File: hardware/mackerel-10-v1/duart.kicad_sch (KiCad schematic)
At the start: 7 parts, among them J2 Conn_01x06, J3 Conn_01x06, U7 XR68C681, X2 3.6864MHz

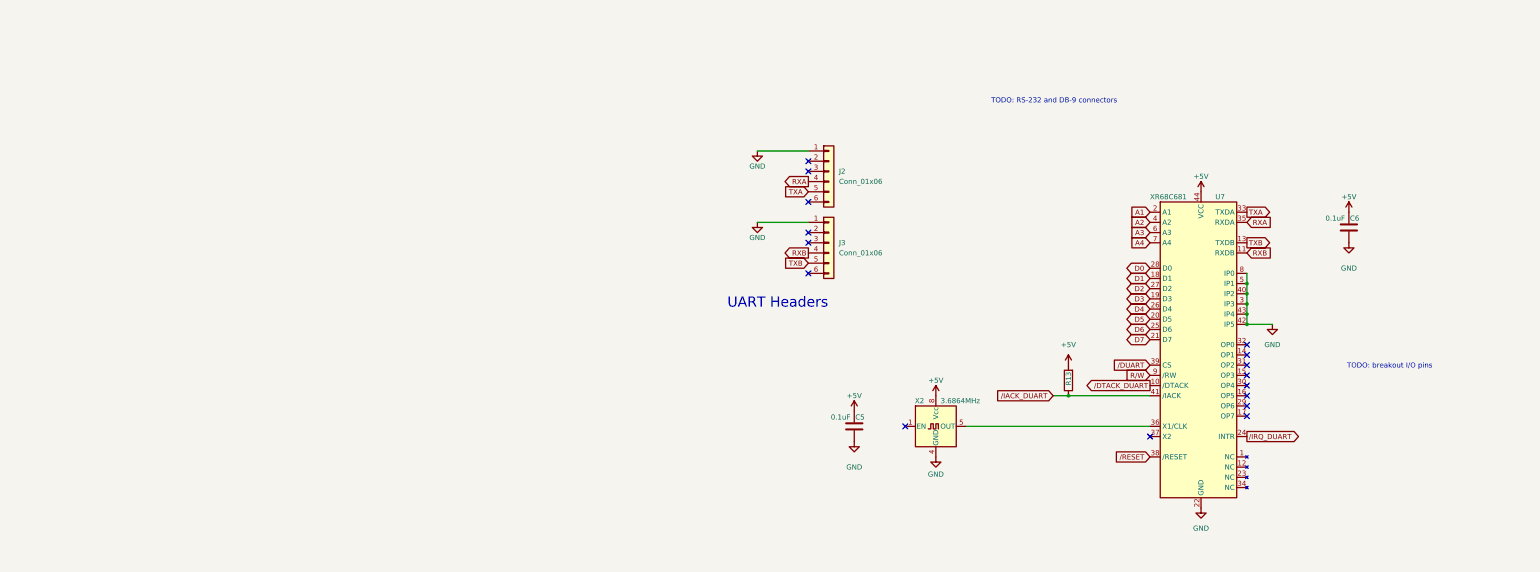
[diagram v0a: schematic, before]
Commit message: Rough layout of components on PCB
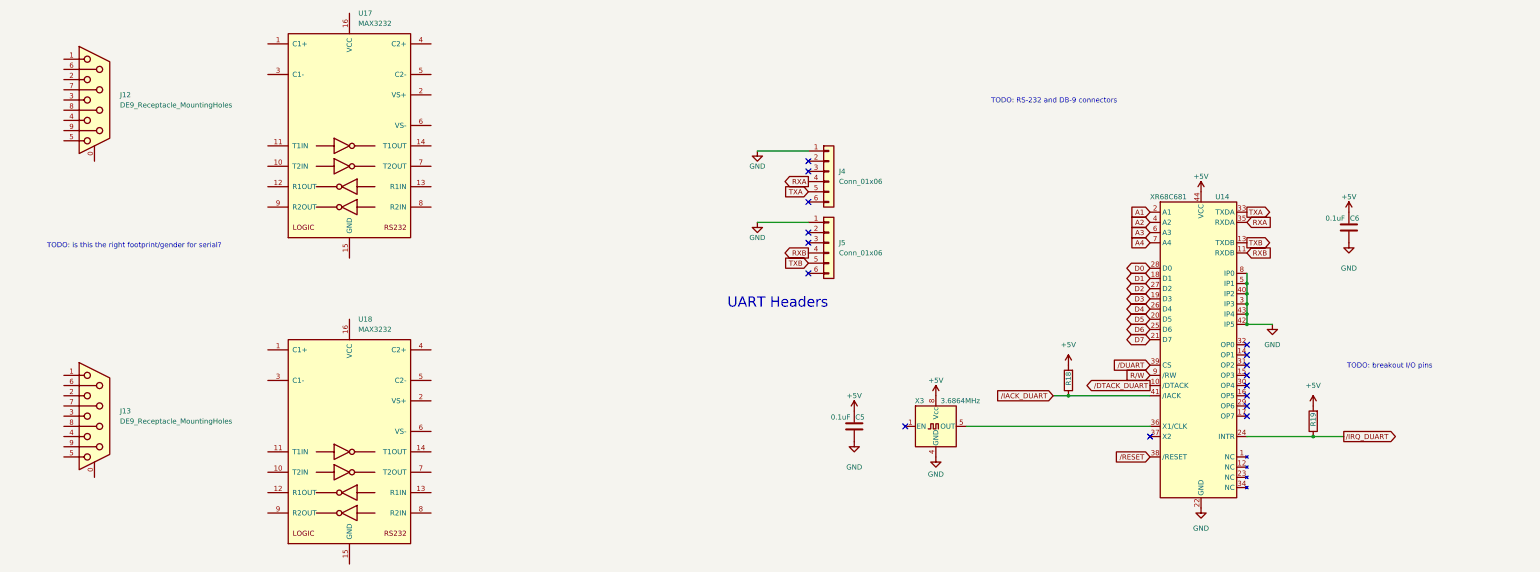
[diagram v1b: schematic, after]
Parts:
- added J12, J13: DE9_Receptacle_MountingHoles, Connector_Dsub:DSUB-9_Female_Horizontal_P2.77x2.84mm_EdgePinOffset7.70mm_Housed_MountingHolesOffset9.12mm, symbol Connector:DE9_Receptacle_MountingHoles
- added R19: R, Resistor_THT:R_Axial_DIN0207_L6.3mm_D2.5mm_P7.62mm_Horizontal, symbol Device:R
- added U17, U18: MAX3232, Package_DIP:DIP-16_W7.62mm_Socket, symbol Interface_UART:MAX3232
- R18: renamed from R13; footprint Resistor_THT:R_Axial_DIN0204_L3.6mm_D1.6mm_P5.08mm_Horizontal -> Resistor_THT:R_Axial_DIN0207_L6.3mm_D2.5mm_P7.62mm_Horizontal
- renumbered J2 to J4, J3 to J5, U7 to U14, X2 to X3
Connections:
- net +5V: now also R19.2
- net /IRQ_DUART: now also R19.1
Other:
- note added: "TODO: is this the right footprint/gender for serial?"

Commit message: Settled on mini ITX form factor
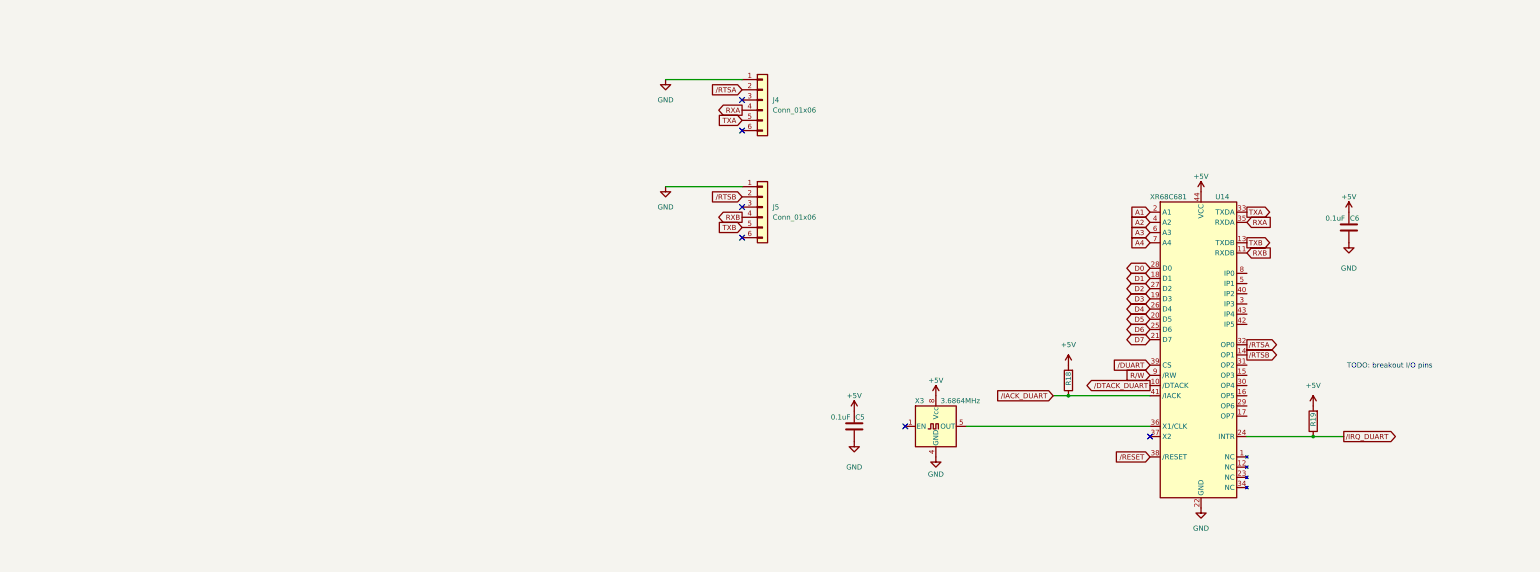
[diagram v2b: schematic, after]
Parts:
- removed J12, J13: DE9_Receptacle_MountingHoles, Connector_Dsub:DSUB-9_Female_Horizontal_P2.77x2.84mm_EdgePinOffset7.70mm_Housed_MountingHolesOffset9.12mm, symbol Connector:DE9_Receptacle_MountingHoles
- removed U17, U18: MAX3232, Package_DIP:DIP-16_W7.62mm_Socket, symbol Interface_UART:MAX3232
- J4, J5: footprint Connector_PinHeader_2.54mm:PinHeader_1x06_P2.54mm_Vertical -> Connector_PinSocket_2.54mm:PinSocket_1x06_P2.54mm_Horizontal
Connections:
- net GND: no longer U14.3 (IP3), U14.40 (IP2), U14.42 (IP5), U14.43 (IP4), U14.5 (IP1), U14.8 (IP0)
- net /RTSA: now reaches J4.2 (Pin_2)
- net /RTSA: now also U14.32 (OP0)
- net /RTSB: now reaches J5.2 (Pin_2)
- net /RTSB: now also U14.14 (OP1)
- no-connect marks 16 -> 6
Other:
- note removed: "TODO: RS-232 and DB-9 connectors"
- note removed: "TODO: is this the right footprint/gender for serial?"
- note removed: "UART Headers"

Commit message: Another layout plan
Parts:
- removed C5, C6: 0.1uF, Capacitor_THT:C_Disc_D4.7mm_W2.5mm_P5.00mm, symbol Device:C
- added J11: Conn_02x08_Odd_Even, Connector_PinHeader_2.54mm:PinHeader_2x08_P2.54mm_Vertical, symbol Connector_Generic:Conn_02x08_Odd_Even
- J4, J5: footprint Connector_PinSocket_2.54mm:PinSocket_1x06_P2.54mm_Horizontal -> Connector_PinSocket_2.54mm:PinSocket_1x06_P2.54mm_Vertical
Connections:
- net +5V: now also J11.1 (Pin_1), J11.2 (Pin_2)
- net GND: now also J11.3 (Pin_3), J11.4 (Pin_4)
- net OP3: now reaches U14.15 (OP3)
- net OP3: now also J11.8 (Pin_8)
- net OP5: now reaches U14.16 (OP5)
- net OP5: now also J11.12 (Pin_12)
- net OP7: now reaches U14.17 (OP7)
- net OP7: now also J11.16 (Pin_16)
- net OP6: now reaches U14.29 (OP6)
- net OP6: now also J11.14 (Pin_14)
- net IP3: now reaches U14.3 (IP3)
- net IP3: now also J11.11 (Pin_11)
- net OP4: now reaches U14.30 (OP4)
- net OP4: now also J11.10 (Pin_10)
- net OP2: now reaches U14.31 (OP2)
- net OP2: now also J11.6 (Pin_6)
- net IP2: now reaches U14.40 (IP2)
- net IP2: now also J11.9 (Pin_9)
- net IP5: now reaches U14.42 (IP5)
- net IP5: now also J11.15 (Pin_15)
- net IP4: now reaches U14.43 (IP4)
- net IP4: now also J11.13 (Pin_13)
- net IP1: now reaches U14.5 (IP1)
- net IP1: now also J11.7 (Pin_7)
- net IP0: now reaches U14.8 (IP0)
- net IP0: now also J11.5 (Pin_5)

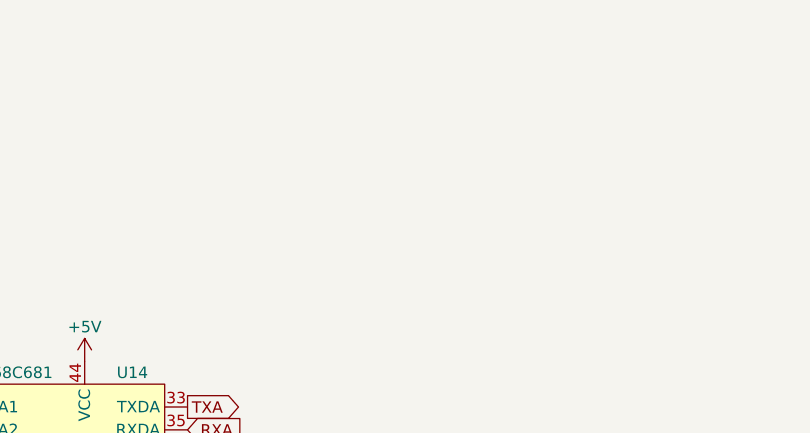
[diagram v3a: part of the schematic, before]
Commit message: half routed
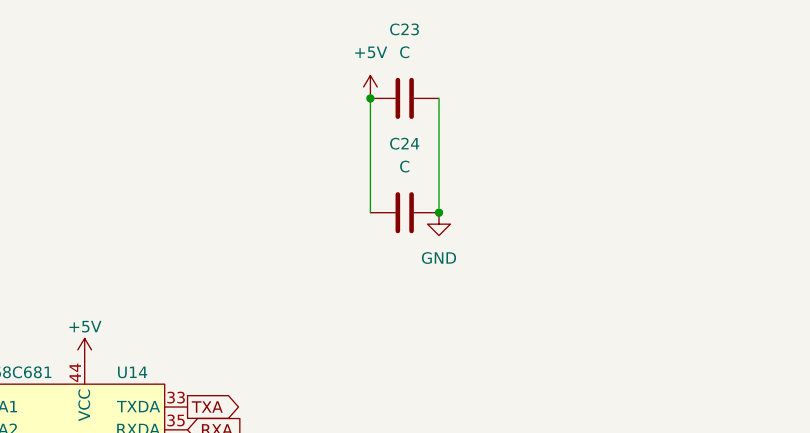
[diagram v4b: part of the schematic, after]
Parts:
- added C23, C24: C, Capacitor_THT:C_Disc_D4.3mm_W1.9mm_P5.00mm, symbol Device:C
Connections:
- net +5V: now also C23.1, C24.1
- net GND: now also C23.2, C24.2

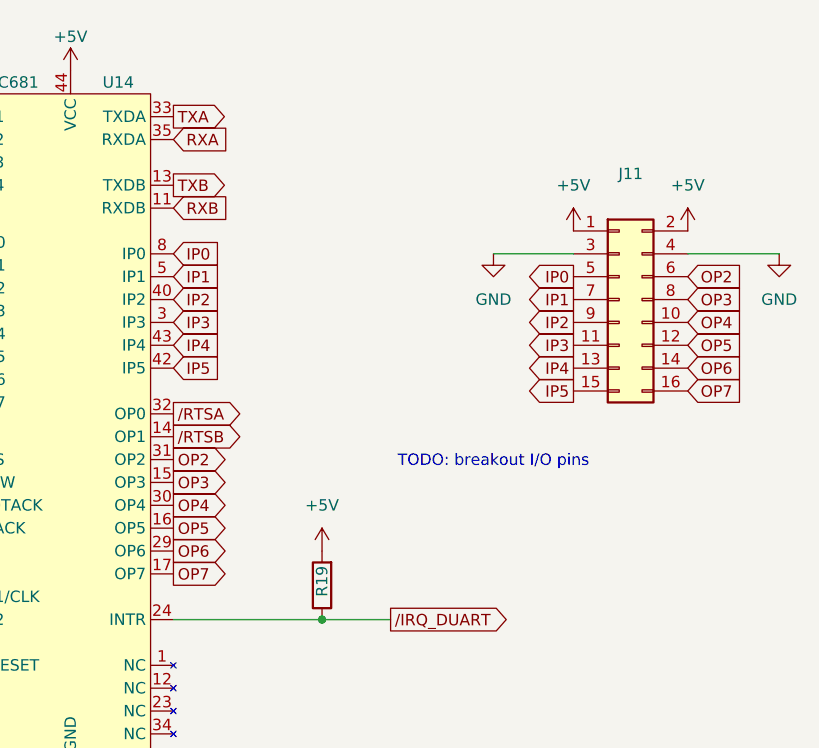
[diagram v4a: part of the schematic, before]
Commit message: DRAM controller mostly routed
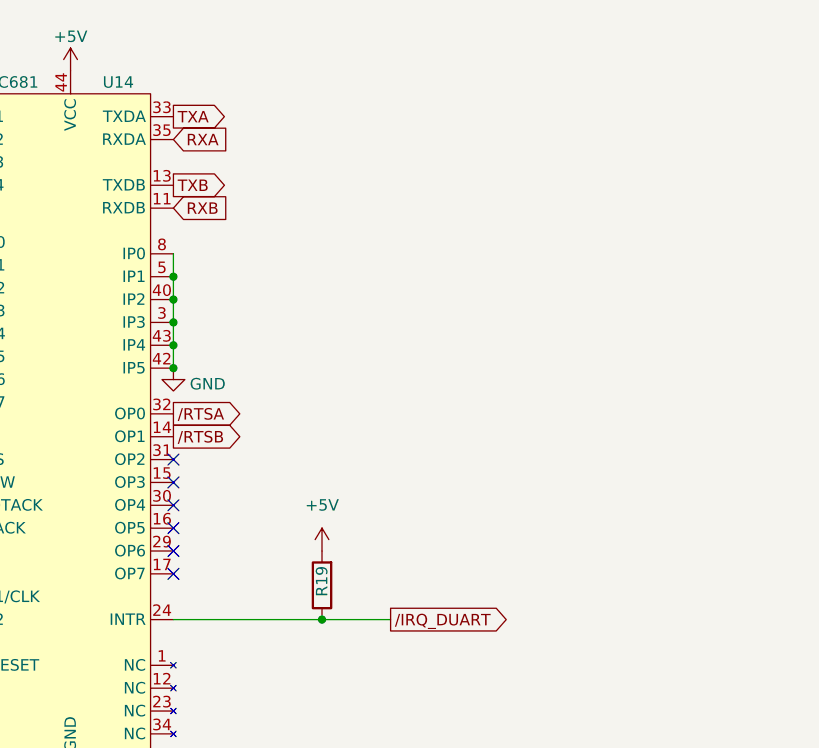
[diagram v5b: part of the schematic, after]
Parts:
- removed J11: Conn_02x08_Odd_Even, Connector_PinHeader_2.54mm:PinHeader_2x08_P2.54mm_Vertical, symbol Connector_Generic:Conn_02x08_Odd_Even
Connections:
- net IP0 is gone; now on net GND: U14.8 (IP0)
- net IP1 is gone; now on net GND: U14.5 (IP1)
- net IP2 is gone; now on net GND: U14.40 (IP2)
- net IP3 is gone; now on net GND: U14.3 (IP3)
- net IP4 is gone; now on net GND: U14.43 (IP4)
- net IP5 is gone; now on net GND: U14.42 (IP5)
- net OP2: no longer names the net of U14.31 (OP2)
- net OP3: no longer names the net of U14.15 (OP3)
- net OP4: no longer names the net of U14.30 (OP4)
- net OP5: no longer names the net of U14.16 (OP5)
- net OP6: no longer names the net of U14.29 (OP6)
- net OP7: no longer names the net of U14.17 (OP7)
- no-connect marks 6 -> 12
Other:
- note removed: "TODO: breakout I/O pins"

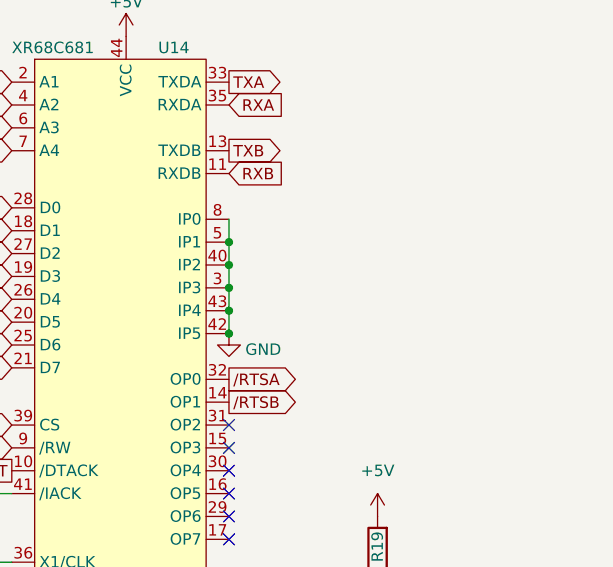
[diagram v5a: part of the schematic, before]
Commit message: IDE interface routed
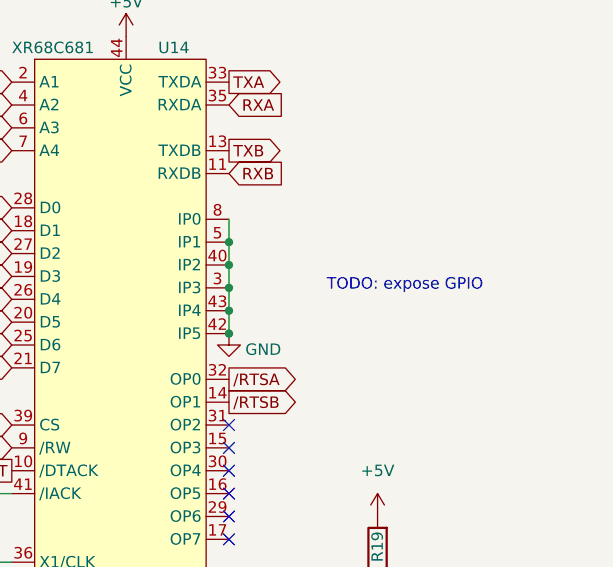
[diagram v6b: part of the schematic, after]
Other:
- note added: "TODO: expose GPIO"
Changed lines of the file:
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@@
+		)
+	)
+	(text "TODO: expose GPIO"
+		(exclude_from_sim no)
+		(at 208.788 86.106 0)
+		(effects
+			(font
+				(size 1.27 1.27)
+			)
 		)
 	)

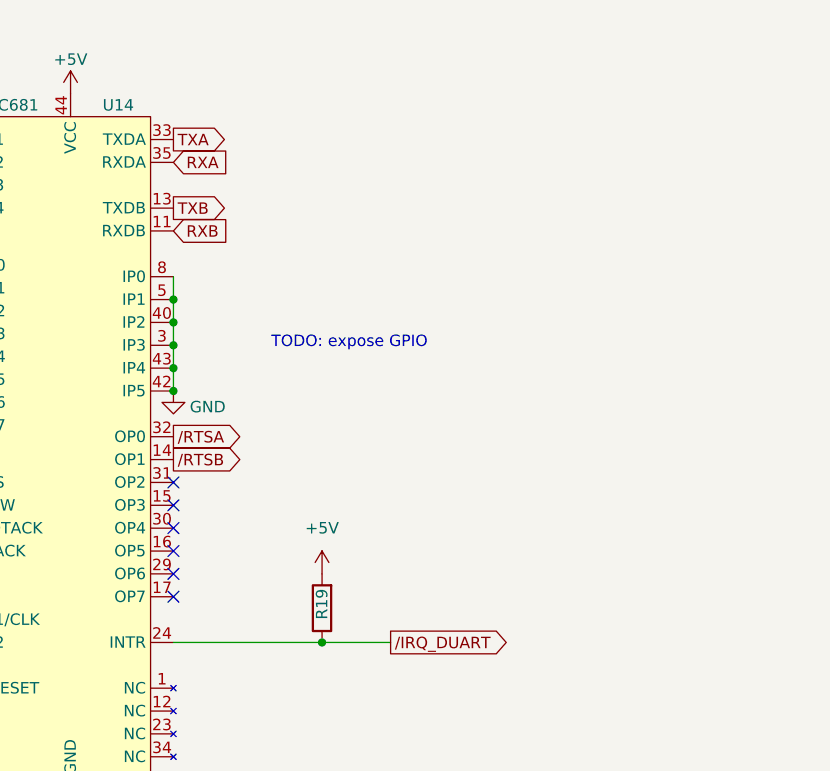
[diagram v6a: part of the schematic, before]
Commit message: Routed DUART GPIO
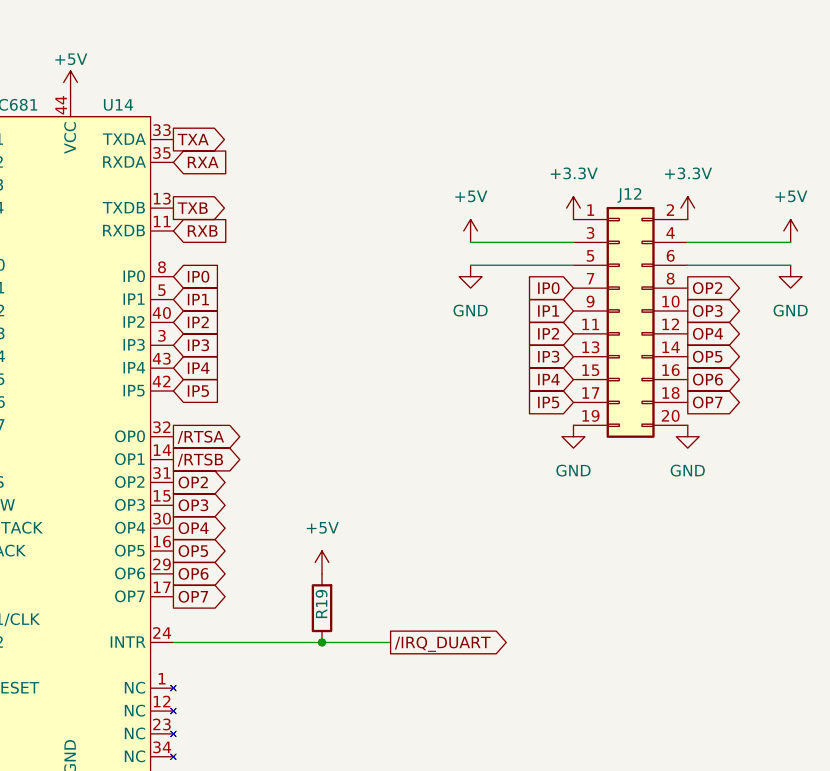
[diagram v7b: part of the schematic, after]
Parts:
- added J12: Conn_02x10_Odd_Even, Connector_PinHeader_2.54mm:PinHeader_2x10_P2.54mm_Vertical, symbol Connector_Generic:Conn_02x10_Odd_Even
- J4, J5: footprint Connector_PinSocket_2.54mm:PinSocket_1x06_P2.54mm_Vertical -> Connector_PinHeader_2.54mm:PinHeader_1x06_P2.54mm_Vertical
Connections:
- net +5V: now also J12.3 (Pin_3), J12.4 (Pin_4)
- net GND: now also J12.19 (Pin_19), J12.20 (Pin_20), J12.5 (Pin_5), J12.6 (Pin_6); no longer U14.3 (IP3), U14.40 (IP2), U14.42 (IP5), U14.43 (IP4), U14.5 (IP1), U14.8 (IP0)
- net OP3: now reaches U14.15 (OP3)
- net OP3: now also J12.10 (Pin_10)
- net OP5: now reaches U14.16 (OP5)
- net OP5: now also J12.14 (Pin_14)
- net OP7: now reaches U14.17 (OP7)
- net OP7: now also J12.18 (Pin_18)
- net OP6: now reaches U14.29 (OP6)
- net OP6: now also J12.16 (Pin_16)
- net OP4: now reaches U14.30 (OP4)
- net OP4: now also J12.12 (Pin_12)
- net OP2: now reaches U14.31 (OP2)
- net OP2: now also J12.8 (Pin_8)
- new net +3.3V: J12.1 (Pin_1), J12.2 (Pin_2)
- new net IP0: J12.7 (Pin_7), U14.8 (IP0)
- new net IP1: J12.9 (Pin_9), U14.5 (IP1)
- new net IP2: J12.11 (Pin_11), U14.40 (IP2)
- new net IP3: J12.13 (Pin_13), U14.3 (IP3)
- new net IP4: J12.15 (Pin_15), U14.43 (IP4)
- new net IP5: J12.17 (Pin_17), U14.42 (IP5)
- no-connect marks 12 -> 6
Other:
- note removed: "TODO: expose GPIO"
